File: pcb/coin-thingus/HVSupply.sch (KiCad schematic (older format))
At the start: 17 parts, among them T1 Sumida-13324-TO86, U2 LT8304

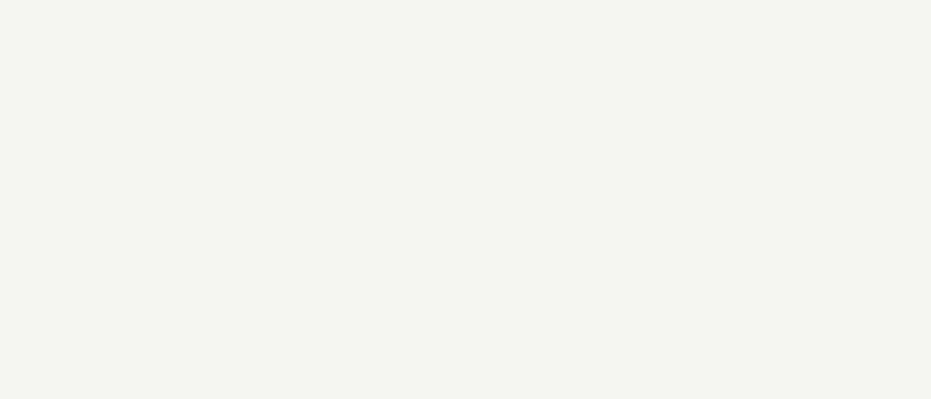
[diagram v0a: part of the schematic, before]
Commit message: Add CERN-OHL-W v2 license
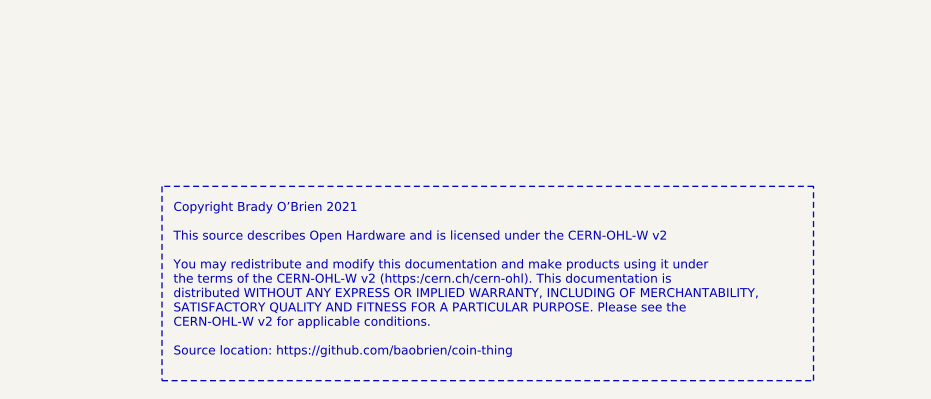
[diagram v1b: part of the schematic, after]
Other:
- note added: "Copyright Brady O’Brien 2021\n\nThis source describes Open Hardware and is licensed under the CERN-OHL-W v2\n\nYou may redistribute and modify this documentation and make products using it under\nthe terms of the CERN-OHL-W v2 (https:/cern.ch/cern-ohl). This documentation is\ndistributed WITHOUT ANY EXPRESS OR IMPLIED WARRANTY, INCLUDING OF MERCHANTABILITY,\nSATISFACTORY QUALITY AND FITNESS FOR A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"
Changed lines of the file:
@@
 	1    0    0    -1
 $EndComp
+Text Notes 8200 6200 0    39   ~ 0
+Copyright Brady O’Brien 2021\n\nThis source describes Open Hardware and is licensed under the CERN-OHL-W v2\n\nYou may redistribute and modify this documentation and make products using it under\nthe terms of the CERN-OHL-W v2 (https:/cern.ch/cern-ohl). This documentation is\ndistributed WITHOUT ANY EXPRESS OR IMPLIED WARRANTY, INCLUDING OF MERCHANTABILITY,\nSATISFACTORY QUALITY AND FITNESS FOR A PARTICULAR PURPOSE. Please see the\nCERN-OHL-W v2 for applicable conditions.\n\nSource location: https://github.com/baobrien/coin-thing
+Wire Notes Line
+	8150 5450 8150 6300
+Wire Notes Line
+	8150 6300 11000 6300
+Wire Notes Line
+	11000 6300 11000 5450
+Wire Notes Line
+	11000 5450 8150 5450
 $EndSCHEMATC

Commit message: Some work towards v0.2
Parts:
- R4: footprint Resistor_SMD:R_0603_1608Metric -> Button_Switch_SMD:SW_SPST_Omron_B3FS-100xP
- R5: footprint Resistor_SMD:R_0603_1608Metric -> Button_Switch_SMD:SW_SPST_TL3342
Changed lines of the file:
@@
 F 0 "R5" H 4932 3954 50  0000 R CNN
 F 1 "10k" H 4932 4045 50  0000 R CNN
-F 2 "Resistor_SMD:R_0603_1608Metric" V 5040 3990 50  0001 C CNN
+F 2 "Button_Switch_SMD:SW_SPST_TL3342" V 5040 3990 50  0001 C CNN
 F 3 "~" H 5000 4000 50  0001 C CNN
 	1    5000 4000
@@
 F 0 "R4" H 4832 2804 50  0000 R CNN
 F 1 "200R" H 4832 2895 50  0000 R CNN
-F 2 "Resistor_SMD:R_0603_1608Metric" V 4940 2840 50  0001 C CNN
+F 2 "Button_Switch_SMD:SW_SPST_Omron_B3FS-100xP" V 4940 2840 50  0001 C CNN
 F 3 "~" H 4900 2850 50  0001 C CNN
 	1    4900 2850

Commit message: HV test board; A bunch of work towards v0.2
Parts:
- added C12: .1u, Capacitor_SMD:C_1210_3225Metric, symbol Device:C
- D2: Part CMMR1U-06 -> (none); part DFLS1150-7 -> (none)
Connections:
- net VOUT_N: now also T1.6 (SB), C12.2; no longer T1.10 (SA)
- net VOUT_P: now also C12.1
- net at D3.2 (A): now also T1.10 (SA); no longer T1.6 (SB)
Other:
- moved on the sheet: C4, D3, TP1, TP2
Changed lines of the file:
@@
 L Device:D D?
 U 1 1 5FA47F8C
-P 6800 3200
+P 6800 3600
 AR Path="/5FA47F8C" Ref="D?"  Part="1"
 AR Path="/5FA3EC89/5FA47F8C" Ref="D3"  Part="1"
-F 0 "D3" H 6800 2984 50  0000 C CNN
-F 1 " CMMR1U-06" H 6800 3075 50  0000 C CNN
-F 2 "Diode_SMD:D_SOD-123F" H 6800 3200 50  0001 C CNN
-F 3 "~" H 6800 3200 50  0001 C CNN
-F 4 " CMMR1U-06" H 6800 3200 50  0001 C CNN "Part"
-	1    6800 3200
-	-1   0    0    1
-$EndComp
-Wire Wire Line
-	6400 3200 6650 3200
+F 0 "D3" H 6800 3384 50  0000 C CNN
+F 1 " CMMR1U-06" H 6950 3500 50  0000 C CNN
+F 2 "Diode_SMD:D_SOD-123F" H 6800 3600 50  0001 C CNN
+F 3 "~" H 6800 3600 50  0001 C CNN
+F 4 " CMMR1U-06" H 6800 3600 50  0001 C CNN "Part"
+	1    6800 3600
+	-1   0    0    1
+$EndComp
 $Comp
 L Device:CP1 C?
 U 1 1 5FA47F93
-P 7250 3400
+P 7650 3400
 AR Path="/5FA47F93" Ref="C?"  Part="1"
 AR Path="/5FA3EC89/5FA47F93" Ref="C4"  Part="1"
-F 0 "C4" H 7365 3446 50  0000 L CNN
-F 1 "1u" H 7365 3355 50  0000 L CNN
-F 2 "Capacitor_THT:CP_Radial_D6.3mm_P2.50mm" H 7250 3400 50  0001 C CNN
-F 3 "~" H 7250 3400 50  0001 C CNN
-	1    7250 3400
-	1    0    0    -1
-$EndComp
-Wire Wire Line
-	6950 3200 7250 3200
-Wire Wire Line
-	7250 3200 7250 3250
-Wire Wire Line
-	6400 3600 7250 3600
-Wire Wire Line
-	7250 3600 7250 3550
+F 0 "C4" H 7765 3446 50  0000 L CNN
+F 1 "1u" H 7765 3355 50  0000 L CNN
+F 2 "Capacitor_THT:CP_Radial_D6.3mm_P2.50mm" H 7650 3400 50  0001 C CNN
+F 3 "~" H 7650 3400 50  0001 C CNN
+	1    7650 3400
+	-1   0    0    1
+$EndComp
 $Comp
 L Device:R_US R?
@@
 AR Path="/5FA3EC89/5FA4800E" Ref="D2"  Part="1"
 F 0 "D2" V 4550 2750 50  0000 C CNN
-F 1 "DFLS1150-7" H 4550 2950 50  0000 C CNN
+F 1 "DFLS1150-7" H 4550 2950 50  0001 C CNN
 F 2 "Diode_SMD:D_PowerDI-123" H 4550 2850 50  0001 C CNN
 F 3 "~" H 4550 2850 50  0001 C CNN
-F 4 " CMMR1U-06" H 4550 2850 50  0001 C CNN "Part"
-F 5 "DFLS1150-7" V 4550 2850 50  0001 C CNN "part"
+F 4 "" H 4550 2850 50  0001 C CNN "Part"
 	1    4550 2850
 	0    1    1    0
@@
 Wire Wire Line
 	4750 3600 4900 3600
-Text Label 7250 3200 2    50   ~ 0
+Text Label 7700 3600 0    50   ~ 0
 HV_P
-Text Label 7250 3600 2    50   ~ 0
+Text Label 7700 3200 0    50   ~ 0
 HV_N
 Text Label 3150 3600 0    50   ~ 0
@@
 Text HLabel 2450 3200 0    50   Input ~ 0
 VIN
-Text HLabel 7550 3150 2    50   Output ~ 0
+Text HLabel 7950 3600 2    50   Output ~ 0
 VOUT_P
-Text HLabel 7550 3600 2    50   Output ~ 0
+Text HLabel 7950 3200 2    50   Output ~ 0
 VOUT_N
 Text HLabel 2450 3700 0    50   Input ~ 0
@@
 Connection ~ 2750 3200
 Wire Wire Line
-	7550 3600 7250 3600
-Connection ~ 7250 3600
-Wire Wire Line
-	7550 3150 7250 3150
-Wire Wire Line
-	7250 3150 7250 3200
-Connection ~ 7250 3200
+	4500 3700 5250 3700
+Wire Wire Line
+	5250 3700 5250 4600
+Wire Wire Line
+	5250 4600 5500 4600
+Wire Wire Line
+	5500 4600 5500 4500
+Wire Wire Line
+	5500 4100 5500 4200
+$Comp
+L Connector:TestPoint TP1
+U 1 1 5FD94D5D
+P 7650 3750
+F 0 "TP1" H 7708 3868 50  0000 L CNN
+F 1 "TestPoint" H 7708 3777 50  0000 L CNN
+F 2 "Connector_Pin:Pin_D1.0mm_L10.0mm" H 7850 3750 50  0001 C CNN
+F 3 "~" H 7850 3750 50  0001 C CNN
+	1    7650 3750
+	-1   0    0    1
+$EndComp
+$Comp
+L Connector:TestPoint TP2
+U 1 1 5FD96635
+P 7650 3100
+F 0 "TP2" H 7592 3126 50  0000 R CNN
+F 1 "TestPoint" H 7592 3217 50  0000 R CNN
+F 2 "Connector_Pin:Pin_D1.0mm_L10.0mm" H 7850 3100 50  0001 C CNN
+F 3 "~" H 7850 3100 50  0001 C CNN
+	1    7650 3100
+	1    0    0    -1
+$EndComp
+$Comp
+L coin_trunker_parts:LT8304 U2
+U 1 1 5FDBECF1
+P 4150 3800
+F 0 "U2" H 4075 3477 50  0000 C CNN
+F 1 "LT8304" H 4075 3386 50  0000 C CNN
+F 2 "Package_SO:TI_SO-PowerPAD-8" H 4150 3800 50  0001 C CNN
+F 3 "" H 4150 3800 50  0001 C CNN
+	1    4150 3800
+	1    0    0    -1
+$EndComp
+$Comp
+L coin_trunker_parts:Sumida-13324-TO86 T1
+U 1 1 5FE539A6
+P 6000 3400
+F 0 "T1" H 6000 3781 50  0000 C CNN
+F 1 "Sumida-13324-TO86" H 6000 3690 50  0000 C CNN
+F 2 "coin-trunker:SUMIDA-S-074-1511" H 6000 3400 50  0001 C CNN
+F 3 "~" H 6000 3400 50  0001 C CNN
+	1    6000 3400
+	1    0    0    -1
+$EndComp
+Text Notes 8200 6200 0    39   ~ 0
+Copyright Brady O’Brien 2021\n\nThis source describes Open Hardware and is licensed under the CERN-OHL-W v2\n\nYou may redistribute and modify this documentation and make products using it under\nthe terms of the CERN-OHL-W v2 (https:/cern.ch/cern-ohl). This documentation is\ndistributed WITHOUT ANY EXPRESS OR IMPLIED WARRANTY, INCLUDING OF MERCHANTABILITY,\nSATISFACTORY QUALITY AND FITNESS FOR A PARTICULAR PURPOSE. Please see the\nCERN-OHL-W v2 for applicable conditions.\n\nSource location: https://github.com/baobrien/coin-thing
+Wire Notes Line
+	8150 5450 8150 6300
+Wire Notes Line
+	8150 6300 11000 6300
+Wire Notes Line
+	11000 6300 11000 5450
+Wire Notes Line
+	11000 5450 8150 5450
+Wire Wire Line
+	7650 3200 7650 3250
+Wire Wire Line
+	7650 3750 7650 3600
+Connection ~ 7650 3600
+Wire Wire Line
+	7650 3600 7650 3550
+Wire Wire Line
+	6650 3600 6400 3600
+Wire Wire Line
+	7950 3200 7650 3200
+Connection ~ 7650 3200
+Wire Wire Line
+	7950 3600 7650 3600
+Wire Wire Line
+	7650 3200 7650 3100
+Wire Wire Line
+	5750 4100 5500 4100
+Wire Wire Line
+	5650 3850 5750 3850
+Wire Wire Line
+	5750 3850 5750 4100
+Connection ~ 5500 4100
+Wire Wire Line
+	5500 4100 5500 4000
 $Comp
 L Device:R_POT_TRIM_US RV1
@@
 	1    0    0    1
 $EndComp
-Wire Wire Line
-	5650 3850 5750 3850
-Wire Wire Line
-	5750 3850 5750 4100
-Wire Wire Line
-	5750 4100 5500 4100
-Wire Wire Line
-	5500 4100 5500 4000
-Wire Wire Line
-	4500 3700 5250 3700
-Wire Wire Line
-	5250 3700 5250 4600
-Wire Wire Line
-	5250 4600 5500 4600
-Wire Wire Line
-	5500 4600 5500 4500
-Wire Wire Line
-	5500 4100 5500 4200
-Connection ~ 5500 4100
-$Comp
-L Connector:TestPoint TP1
-U 1 1 5FD94D5D
-P 7250 3050
-F 0 "TP1" H 7308 3168 50  0000 L CNN
-F 1 "TestPoint" H 7308 3077 50  0000 L CNN
-F 2 "Connector_Pin:Pin_D1.0mm_L10.0mm" H 7450 3050 50  0001 C CNN
-F 3 "~" H 7450 3050 50  0001 C CNN
-	1    7250 3050
-	1    0    0    -1
-$EndComp
-Wire Wire Line
-	7250 3050 7250 3150
-Connection ~ 7250 3150
-$Comp
-L Connector:TestPoint TP2
-U 1 1 5FD96635
-P 7250 3700
-F 0 "TP2" H 7192 3726 50  0000 R CNN
-F 1 "TestPoint" H 7192 3817 50  0000 R CNN
-F 2 "Connector_Pin:Pin_D1.0mm_L10.0mm" H 7450 3700 50  0001 C CNN
-F 3 "~" H 7450 3700 50  0001 C CNN
-	1    7250 3700
-	-1   0    0    1
-$EndComp
-Wire Wire Line
-	7250 3700 7250 3600
-$Comp
-L coin_trunker_parts:LT8304 U2
-U 1 1 5FDBECF1
-P 4150 3800
-F 0 "U2" H 4075 3477 50  0000 C CNN
-F 1 "LT8304" H 4075 3386 50  0000 C CNN
-F 2 "Package_SO:TI_SO-PowerPAD-8" H 4150 3800 50  0001 C CNN
-F 3 "" H 4150 3800 50  0001 C CNN
-	1    4150 3800
-	1    0    0    -1
-$EndComp
-$Comp
-L coin_trunker_parts:Sumida-13324-TO86 T1
-U 1 1 5FE539A6
-P 6000 3400
-F 0 "T1" H 6000 3781 50  0000 C CNN
-F 1 "Sumida-13324-TO86" H 6000 3690 50  0000 C CNN
-F 2 "coin-trunker:SUMIDA-S-074-1511" H 6000 3400 50  0001 C CNN
-F 3 "~" H 6000 3400 50  0001 C CNN
-	1    6000 3400
-	1    0    0    -1
-$EndComp
-Text Notes 8200 6200 0    39   ~ 0
-Copyright Brady O’Brien 2021\n\nThis source describes Open Hardware and is licensed under the CERN-OHL-W v2\n\nYou may redistribute and modify this documentation and make products using it under\nthe terms of the CERN-OHL-W v2 (https:/cern.ch/cern-ohl). This documentation is\ndistributed WITHOUT ANY EXPRESS OR IMPLIED WARRANTY, INCLUDING OF MERCHANTABILITY,\nSATISFACTORY QUALITY AND FITNESS FOR A PARTICULAR PURPOSE. Please see the\nCERN-OHL-W v2 for applicable conditions.\n\nSource location: https://github.com/baobrien/coin-thing
-Wire Notes Line
-	8150 5450 8150 6300
-Wire Notes Line
-	8150 6300 11000 6300
-Wire Notes Line
-	11000 6300 11000 5450
-Wire Notes Line
-	11000 5450 8150 5450
+$Comp
+L Device:C C12
+U 1 1 6057A993
+P 7150 3400
+F 0 "C12" H 7350 3300 50  0000 R CNN
+F 1 ".1u" H 7300 3500 50  0000 R CNN
+F 2 "Capacitor_SMD:C_1210_3225Metric" H 7188 3250 50  0001 C CNN
+F 3 "~" H 7150 3400 50  0001 C CNN
+	1    7150 3400
+	-1   0    0    1
+$EndComp
+Wire Wire Line
+	7150 3600 7150 3550
+Wire Wire Line
+	7150 3600 7650 3600
+Wire Wire Line
+	7150 3600 6950 3600
+Connection ~ 7150 3600
+Wire Wire Line
+	6400 3200 7150 3200
+Wire Wire Line
+	7150 3250 7150 3200
+Connection ~ 7150 3200
+Wire Wire Line
+	7150 3200 7650 3200
 $EndSCHEMATC

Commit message: Bunch'o work towards v0.2
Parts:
- removed RV1: 100K, Potentiometer_SMD:Potentiometer_Bourns_3224X_Vertical, symbol Device:R_POT_TRIM_US
- R3: value 100k -> 130k
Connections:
- net VIN: now also T1.5 (AB); no longer T1.3 (AA)
- net VOUT_N: now also C12.1, R3.1, T1.10 (SA); no longer C12.2, T1.6 (SB)
- net VOUT_P: now also C12.2, R3.2; no longer C12.1
- net at D3.2 (A): now also T1.6 (SB); no longer T1.10 (SA)
- net at R6.1: now also D2.2 (A), R4.1, T1.3 (AA), U2.5 (SW)
- net at R5.2, U2.7 (Rref): no longer R3.2
- net at U2.8 (Tc): no longer R3.1
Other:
- moved on the sheet: R6
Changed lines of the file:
@@
 AR Path="/5FA47F93" Ref="C?"  Part="1"
 AR Path="/5FA3EC89/5FA47F93" Ref="C4"  Part="1"
-F 0 "C4" H 7765 3446 50  0000 L CNN
-F 1 "1u" H 7765 3355 50  0000 L CNN
+F 0 "C4" H 7450 3450 50  0000 L CNN
+F 1 "1u" H 7450 3350 50  0000 L CNN
 F 2 "Capacitor_THT:CP_Radial_D6.3mm_P2.50mm" H 7650 3400 50  0001 C CNN
 F 3 "~" H 7650 3400 50  0001 C CNN
@@
 L Device:R_US R?
 U 1 1 5FA47F9D
-P 5500 4350
+P 5500 3850
 AR Path="/5FA47F9D" Ref="R?"  Part="1"
 AR Path="/5FA3EC89/5FA47F9D" Ref="R6"  Part="1"
-F 0 "R6" H 5568 4396 50  0000 L CNN
-F 1 "260k" H 5568 4305 50  0000 L CNN
-F 2 "Resistor_SMD:R_0603_1608Metric" V 5540 4340 50  0001 C CNN
-F 3 "~" H 5500 4350 50  0001 C CNN
-	1    5500 4350
+F 0 "R6" H 5568 3896 50  0000 L CNN
+F 1 "260k" H 5568 3805 50  0000 L CNN
+F 2 "Resistor_SMD:R_0603_1608Metric" V 5540 3840 50  0001 C CNN
+F 3 "~" H 5500 3850 50  0001 C CNN
+	1    5500 3850
 	1    0    0    -1
 $EndComp
@@
 	-1   0    0    1
 $EndComp
-$Comp
-L Device:R_US R?
-U 1 1 5FA47FA9
-P 4700 4000
-AR Path="/5FA47FA9" Ref="R?"  Part="1"
-AR Path="/5FA3EC89/5FA47FA9" Ref="R3"  Part="1"
-F 0 "R3" H 4632 3954 50  0000 R CNN
-F 1 "100k" H 4632 4045 50  0000 R CNN
-F 2 "Resistor_SMD:R_0603_1608Metric" V 4740 3990 50  0001 C CNN
-F 3 "~" H 4700 4000 50  0001 C CNN
-	1    4700 4000
-	-1   0    0    1
-$EndComp
-Wire Wire Line
-	5500 3700 5500 3600
-Connection ~ 5500 3600
-Wire Wire Line
-	5500 3600 5600 3600
-Wire Wire Line
-	4500 3800 4700 3800
-Wire Wire Line
-	4700 3800 4700 3850
-Wire Wire Line
-	4500 3900 4550 3900
-Wire Wire Line
-	4550 3900 4550 4250
-Wire Wire Line
-	4550 4250 4700 4250
-Wire Wire Line
-	4700 4250 4700 4150
-Wire Wire Line
-	4700 3800 5000 3800
 Wire Wire Line
 	5000 3800 5000 3850
-Connection ~ 4700 3800
 $Comp
 L power:GND #PWR?
@@
 	4900 3000 4900 3600
 Connection ~ 4900 3600
-Wire Wire Line
-	4900 3600 5500 3600
 Wire Wire Line
 	5250 3000 5250 3200
@@
 Wire Wire Line
 	4500 3700 5250 3700
-Wire Wire Line
-	5250 3700 5250 4600
-Wire Wire Line
-	5250 4600 5500 4600
-Wire Wire Line
-	5500 4600 5500 4500
-Wire Wire Line
-	5500 4100 5500 4200
 $Comp
 L Connector:TestPoint TP1
@@
 F 3 "~" H 6000 3400 50  0001 C CNN
 	1    6000 3400
-	1    0    0    -1
+	1    0    0    1
 $EndComp
 Text Notes 8200 6200 0    39   ~ 0
@@
 Wire Wire Line
 	7650 3200 7650 3100
-Wire Wire Line
-	5750 4100 5500 4100
-Wire Wire Line
-	5650 3850 5750 3850
-Wire Wire Line
-	5750 3850 5750 4100
-Connection ~ 5500 4100
-Wire Wire Line
-	5500 4100 5500 4000
-$Comp
-L Device:R_POT_TRIM_US RV1
-U 1 1 5FD8194F
-P 5500 3850
-F 0 "RV1" H 5433 3804 50  0000 R CNN
-F 1 "100K" H 5750 3750 50  0000 R CNN
-F 2 "Potentiometer_SMD:Potentiometer_Bourns_3224X_Vertical" H 5500 3850 50  0001 C CNN
-F 3 "~" H 5500 3850 50  0001 C CNN
-F 4 "ST4ETB104" H 5500 3850 50  0001 C CNN "Part"
-	1    5500 3850
-	1    0    0    1
-$EndComp
 $Comp
 L Device:C C12
@@
 F 3 "~" H 7150 3400 50  0001 C CNN
 	1    7150 3400
-	-1   0    0    1
+	-1   0    0    -1
 $EndComp
 Wire Wire Line
 	7150 3600 7150 3550
-Wire Wire Line
-	7150 3600 7650 3600
 Wire Wire Line
 	7150 3600 6950 3600
@@
 Connection ~ 7150 3200
 Wire Wire Line
-	7150 3200 7650 3200
+	7150 3200 7350 3200
+Wire Wire Line
+	4900 3600 5500 3600
+Wire Wire Line
+	5500 4000 5500 4100
+Wire Wire Line
+	5500 4100 5250 4100
+Wire Wire Line
+	5250 4100 5250 3700
+Wire Wire Line
+	5500 3700 5500 3600
+Connection ~ 5500 3600
+Wire Wire Line
+	5500 3600 5600 3600
+Wire Wire Line
+	4500 3800 5000 3800
+$Comp
+L Device:R_US R?
+U 1 1 609006DB
+P 7350 3400
+AR Path="/609006DB" Ref="R?"  Part="1"
+AR Path="/5FA3EC89/609006DB" Ref="R3"  Part="1"
+F 0 "R3" H 7418 3446 50  0000 L CNN
+F 1 "130k" H 7400 3300 50  0000 L CNN
+F 2 "Resistor_SMD:R_0603_1608Metric" V 7390 3390 50  0001 C CNN
+F 3 "~" H 7350 3400 50  0001 C CNN
+	1    7350 3400
+	1    0    0    -1
+$EndComp
+Wire Wire Line
+	7350 3550 7350 3600
+Wire Wire Line
+	7150 3600 7350 3600
+Connection ~ 7350 3600
+Wire Wire Line
+	7350 3600 7650 3600
+Wire Wire Line
+	7350 3250 7350 3200
+Connection ~ 7350 3200
+Wire Wire Line
+	7350 3200 7650 3200
 $EndSCHEMATC

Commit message: Coin thing v0.2 PCB
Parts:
- D3: value CMMR1U-06 -> CMMR1U-06 / 1N4007W
- R6: value 260k -> 240k
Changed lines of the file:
@@
 AR Path="/5FA3EC89/5FA47F8C" Ref="D3"  Part="1"
 F 0 "D3" H 6800 3384 50  0000 C CNN
-F 1 " CMMR1U-06" H 6950 3500 50  0000 C CNN
+F 1 " CMMR1U-06 / 1N4007W" H 6950 3900 50  0000 C CNN
 F 2 "Diode_SMD:D_SOD-123F" H 6800 3600 50  0001 C CNN
 F 3 "~" H 6800 3600 50  0001 C CNN
@@
 AR Path="/5FA3EC89/5FA47F9D" Ref="R6"  Part="1"
 F 0 "R6" H 5568 3896 50  0000 L CNN
-F 1 "260k" H 5568 3805 50  0000 L CNN
+F 1 "240k" H 5568 3805 50  0000 L CNN
 F 2 "Resistor_SMD:R_0603_1608Metric" V 5540 3840 50  0001 C CNN
 F 3 "~" H 5500 3850 50  0001 C CNN

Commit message: V0.2 as ordered
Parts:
- D3: Part CMMR1U-06 -> CMMR1U-06
- R4: footprint Button_Switch_SMD:SW_SPST_Omron_B3FS-100xP -> Resistor_SMD:R_0603_1608Metric
- R5: footprint Button_Switch_SMD:SW_SPST_TL3342 -> Resistor_SMD:R_0603_1608Metric
- U2: value LT8304 -> LT8304-1
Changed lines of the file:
@@
 F 2 "Diode_SMD:D_SOD-123F" H 6800 3600 50  0001 C CNN
 F 3 "~" H 6800 3600 50  0001 C CNN
-F 4 " CMMR1U-06" H 6800 3600 50  0001 C CNN "Part"
+F 4 "CMMR1U-06" H 6800 3600 50  0001 C CNN "Part"
 	1    6800 3600
 	-1   0    0    1
@@
 F 0 "R5" H 4932 3954 50  0000 R CNN
 F 1 "10k" H 4932 4045 50  0000 R CNN
-F 2 "Button_Switch_SMD:SW_SPST_TL3342" V 5040 3990 50  0001 C CNN
+F 2 "Resistor_SMD:R_0603_1608Metric" V 5040 3990 50  0001 C CNN
 F 3 "~" H 5000 4000 50  0001 C CNN
 	1    5000 4000
@@
 F 0 "R4" H 4832 2804 50  0000 R CNN
 F 1 "200R" H 4832 2895 50  0000 R CNN
-F 2 "Button_Switch_SMD:SW_SPST_Omron_B3FS-100xP" V 4940 2840 50  0001 C CNN
+F 2 "Resistor_SMD:R_0603_1608Metric" V 4940 2840 50  0001 C CNN
 F 3 "~" H 4900 2850 50  0001 C CNN
 	1    4900 2850
@@
 P 4150 3800
 F 0 "U2" H 4075 3477 50  0000 C CNN
-F 1 "LT8304" H 4075 3386 50  0000 C CNN
+F 1 "LT8304-1" H 4075 3386 50  0000 C CNN
 F 2 "Package_SO:TI_SO-PowerPAD-8" H 4150 3800 50  0001 C CNN
 F 3 "" H 4150 3800 50  0001 C CNN

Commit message: Start work on alternate micro
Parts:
- R2, R3, R4, R5: footprint Resistor_SMD:R_0603_1608Metric -> Resistor_SMD:R_0402_1005Metric
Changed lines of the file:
@@
 F 0 "R5" H 4932 3954 50  0000 R CNN
 F 1 "10k" H 4932 4045 50  0000 R CNN
-F 2 "Resistor_SMD:R_0603_1608Metric" V 5040 3990 50  0001 C CNN
+F 2 "Resistor_SMD:R_0402_1005Metric" V 5040 3990 50  0001 C CNN
 F 3 "~" H 5000 4000 50  0001 C CNN
 	1    5000 4000
@@
 F 0 "R4" H 4832 2804 50  0000 R CNN
 F 1 "200R" H 4832 2895 50  0000 R CNN
-F 2 "Resistor_SMD:R_0603_1608Metric" V 4940 2840 50  0001 C CNN
+F 2 "Resistor_SMD:R_0402_1005Metric" V 4940 2840 50  0001 C CNN
 F 3 "~" H 4900 2850 50  0001 C CNN
 	1    4900 2850
@@
 F 0 "R2" H 3032 3354 50  0000 R CNN
 F 1 "10k" H 3032 3445 50  0000 R CNN
-F 2 "Resistor_SMD:R_0603_1608Metric" V 3140 3390 50  0001 C CNN
+F 2 "Resistor_SMD:R_0402_1005Metric" V 3140 3390 50  0001 C CNN
 F 3 "~" H 3100 3400 50  0001 C CNN
 	1    3100 3400
@@
 F 0 "R3" H 7418 3446 50  0000 L CNN
 F 1 "130k" H 7400 3300 50  0000 L CNN
-F 2 "Resistor_SMD:R_0603_1608Metric" V 7390 3390 50  0001 C CNN
+F 2 "Resistor_SMD:R_0402_1005Metric" V 7390 3390 50  0001 C CNN
 F 3 "~" H 7350 3400 50  0001 C CNN
 	1    7350 3400
